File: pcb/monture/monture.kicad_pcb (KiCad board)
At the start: 2 copper layers, 145 x 100 mm, 32 parts, among them U1 Teensy 4.1

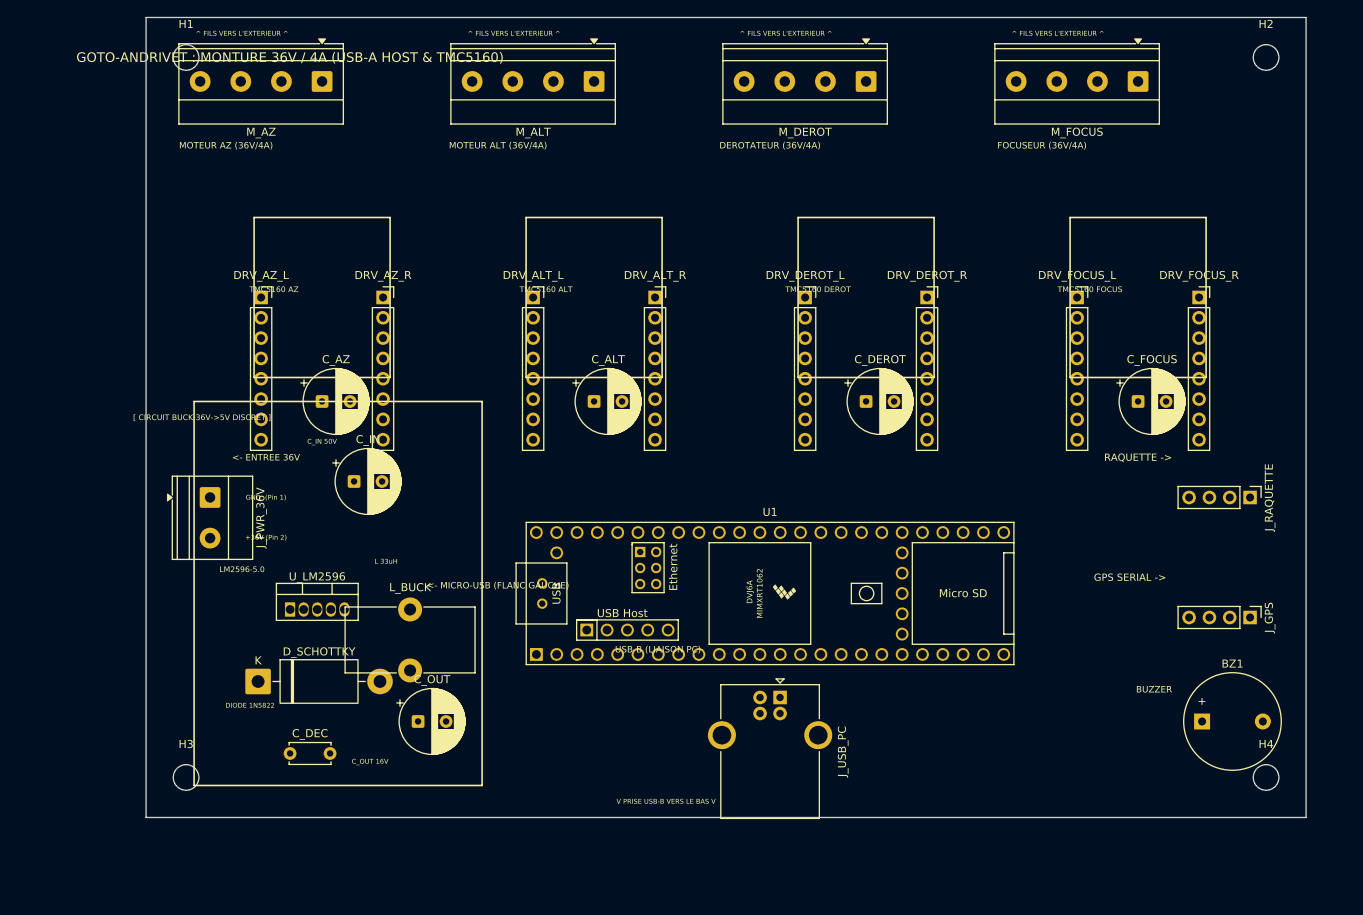
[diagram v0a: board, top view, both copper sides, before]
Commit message: Optimisation dimensions PCB (150x110mm) et centrage parfait de tous les connecteurs
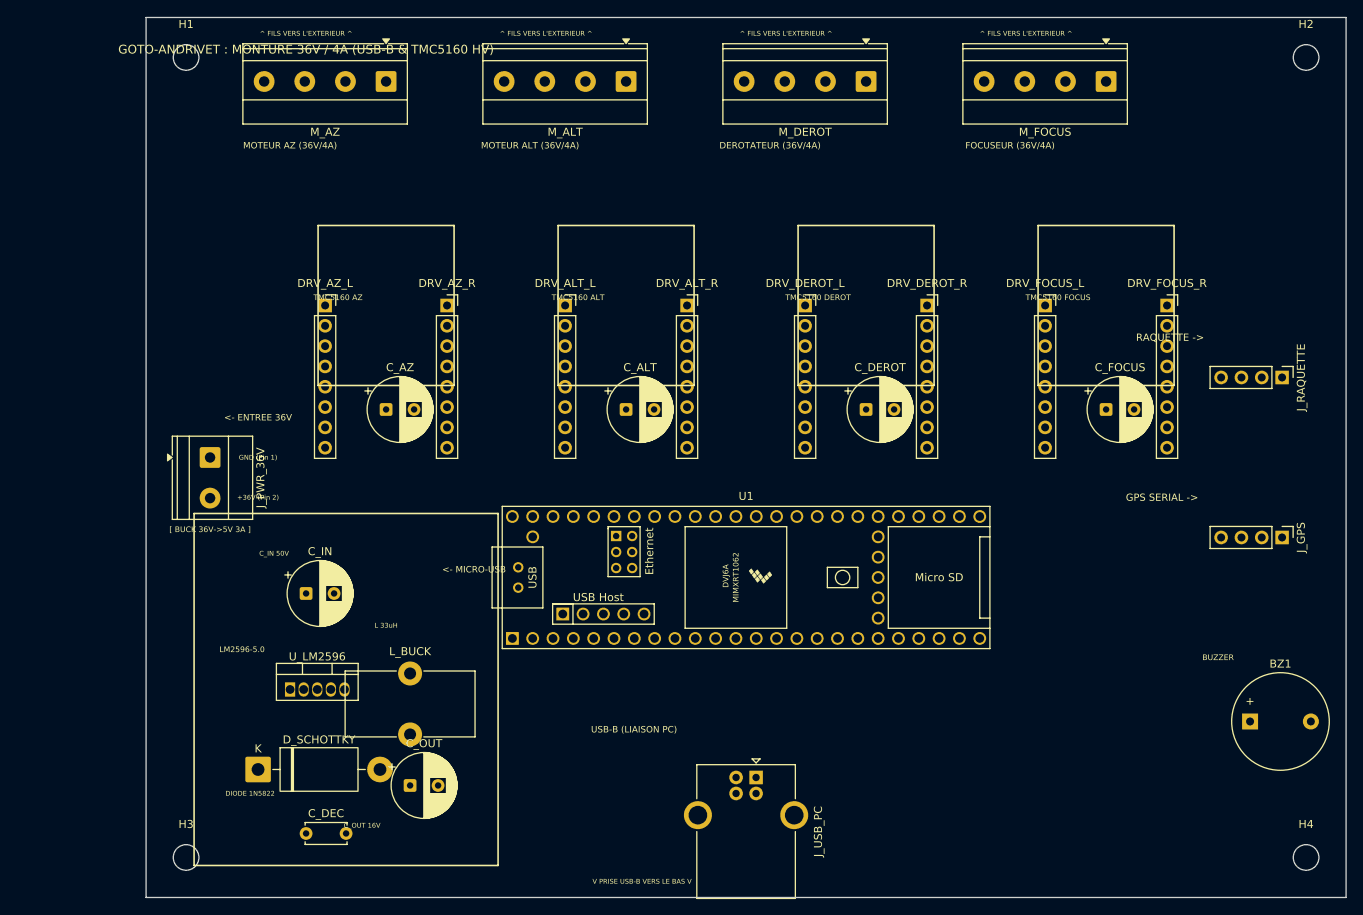
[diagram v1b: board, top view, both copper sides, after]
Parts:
- C_ALT, C_AZ, C_DEROT, C_FOCUS: value 470uF 50V/63V -> 470uF 63V
- C_OUT: value 470uF 16V -> 220uF 16V
- L_BUCK: value 33uH-47uH 3A -> 33uH 3A
- moved J_RAQUETTE 15.5 mm to (142.0, 45.0)
- moved C_IN 15.2 mm to (20.0, 72.0)
- moved H4 11.2 mm to (145.0, 105.0)
- moved D_SCHOTTKY 11.0 mm to (14.0, 94.0)
- moved J_GPS 10.8 mm to (142.0, 65.0)
- moved J_USB_PC 10.4 mm to (76.2, 95.0)
- moved C_DEC 10.2 mm to (20.0, 102.0)
- moved H3 10.0 mm to (5.00, 105.0)
- moved U_LM2596 10.0 mm to (18.0, 84.0)
- moved DRV_AZ_L 8.06 mm to (22.4, 36.0)
- moved C_AZ 8.06 mm to (30.0, 49.0)
- moved C_OUT 8.06 mm to (33.0, 96.0)
- moved DRV_AZ_R 8.06 mm to (37.6, 36.0)
- moved L_BUCK 8.00 mm to (33.0, 82.0)
- moved M_AZ 8.00 mm to (30.0, 8.00)
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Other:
- board size 145 x 100 mm -> 150 x 110 mm
- board text added: "<- MICRO-USB"
- board text added: "GOTO-ANDRIVET : MONTURE 36V / 4A (USB-B & TMC5160 HV)"
- board text added: "[ BUCK 36V->5V 3A ]"
- board text removed: "<- MICRO-USB (FLANC GAUCHE)"
- board text removed: "GOTO-ANDRIVET : MONTURE 36V / 4A (USB-A HOST & TMC5160)"
- board text removed: "[ CIRCUIT BUCK 36V->5V DISCRET ]"

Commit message: Ajout du repérage explicite des bobines 1 et 2 sur les borniers moteurs et guide de câblage
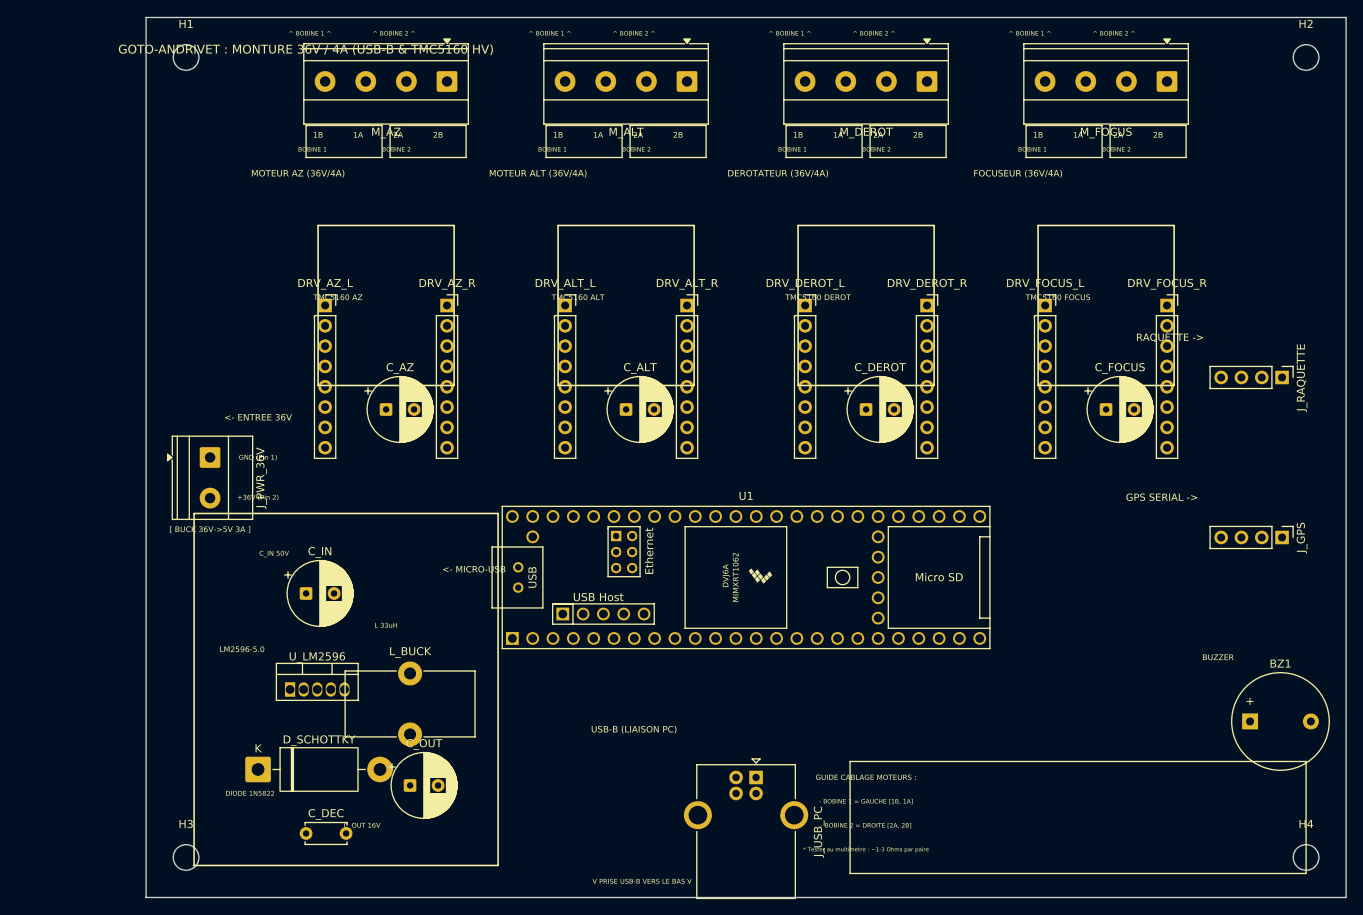
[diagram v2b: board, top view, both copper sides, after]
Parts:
- moved M_ALT 7.62 mm to (67.6, 8.00)
- moved M_DEROT 7.62 mm to (97.6, 8.00)
- moved M_FOCUS 7.62 mm to (127.6, 8.00)
- moved M_AZ 7.62 mm to (37.6, 8.00)
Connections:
- M_ALT pad 1: ALT_1B -> ALT_2B
- M_ALT pad 2: ALT_1A -> ALT_2A
- M_ALT pad 3: ALT_2A -> ALT_1A
- M_ALT pad 4: ALT_2B -> ALT_1B
- M_AZ pad 1: AZ_1B -> AZ_2B
- M_AZ pad 2: AZ_1A -> AZ_2A
- M_AZ pad 3: AZ_2A -> AZ_1A
- M_AZ pad 4: AZ_2B -> AZ_1B
- M_DEROT pad 1: DEROT_1B -> DEROT_2B
- M_DEROT pad 2: DEROT_1A -> DEROT_2A
- M_DEROT pad 3: DEROT_2A -> DEROT_1A
- M_DEROT pad 4: DEROT_2B -> DEROT_1B
- M_FOCUS pad 1: FOCUS_1B -> FOCUS_2B
- M_FOCUS pad 2: FOCUS_1A -> FOCUS_2A
- M_FOCUS pad 3: FOCUS_2A -> FOCUS_1A
- M_FOCUS pad 4: FOCUS_2B -> FOCUS_1B
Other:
- board text added: "* Tester au multimetre : ~1-3 Ohms par paire"
- board text added: "- BOBINE 1 = GAUCHE [1B, 1A]"
- board text added: "- BOBINE 2 = DROITE [2A, 2B]"
- board text added: "1A"
- board text added: "1B"
- board text added: "2A"
- board text added: "2B"
- board text added: "BOBINE 1"
- board text added: "BOBINE 2"
- board text added: "GUIDE CABLAGE MOTEURS :"
- board text added: "^ BOBINE 1 ^"
- board text added: "^ BOBINE 2 ^"
- board text removed: "^ FILS VERS L'EXTERIEUR ^"

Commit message: Alignement vertical des connecteurs Raquette et GPS avec repérage complet des broches
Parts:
- moved J_GPS 3.81 mm to (142.0, 61.2), turned to 0 degrees
- moved J_RAQUETTE 3.81 mm to (142.0, 41.2), turned to 0 degrees
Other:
- board text added: "1: GND"
- board text added: "1: RX <- TX"
- board text added: "2: +5V"
- board text added: "2: TX -> RX"
- board text added: "3: +5V"
- board text added: "3: RX"
- board text added: "4: GND"
- board text added: "4: TX"
- board text added: "[ GPS SERIAL ]"
- board text added: "[ RAQUETTE ]"
- board text removed: "GPS SERIAL ->"
- board text removed: "RAQUETTE ->"

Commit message: Intégration du Teensy 4.1 avec barrettes de broches et sockets 3D, et inductance de puissance radiale
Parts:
- removed the L_BUCK at (33.0, 82.0)
- added L_BUCK: 33uH 3A, L_Radial_D12.5mm_P7.00mm_Fastron_09HCP, F.Cu at (33.0, 82.0)

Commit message: pcb(monture): Routage physique des pistes USB Host du Teensy 4.1 vers USB-B
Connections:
- U1 pad 59: (no net) -> GND
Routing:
- net GND: track 0.00 -> 81.2 mm
- net +5V: track 0.00 -> 43.1 mm
- net USB_HOST_DM: track 0.00 -> 38.1 mm
- net USB_HOST_DP: track 0.00 -> 37.5 mm, vias 0 -> 1
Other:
- board text added: "USB-B (LIAISON / HOST)"
- board text removed: "USB-B (LIAISON PC)"
